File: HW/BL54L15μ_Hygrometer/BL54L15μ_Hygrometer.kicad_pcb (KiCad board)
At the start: 2 copper layers, 25.4 x 25.4 mm, 21 parts, among them IC1 nrf54L 453-00223R, J1 Conn_Qwiic, J2 Conn_ARM_JTAG_SWD_10, U1 nPM2100-QEXX, U2 SHT4x, U3 STCC4-D-R3, U5 BME688, X1 32.768 kHz

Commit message: BL54L15μ Hygrometer 2026v3
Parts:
- added JP1: VSET-GND, Jumper:SolderJumper-2_P1.3mm_Open_RoundedPad1.0x1.5mm, B.Cu at (103.9, 58.6)
- added SW1: Reset, Button_Switch_SMD:SW_Push_SPST_NO_Alps_SKRK, F.Cu at (102.3, 69.7)
- added TP1: VDD, TestPoint:TestPoint_Pad_D1.0mm, B.Cu at (108.0, 63.5)
- added TP10: PG/RESET, TestPoint:TestPoint_Pad_D1.0mm, B.Cu at (103.6, 66.8)
- added TP11: SYSGDEN, TestPoint:TestPoint_Pad_D1.0mm, B.Cu at (99.1, 66.8)
- added TP12: LED0, TestPoint:TestPoint_Pad_D1.0mm, B.Cu at (108.0, 74.2)
- added TP13: VDDSW, TestPoint:TestPoint_Pad_D1.0mm, B.Cu at (110.2, 63.5)
- added TP2: GND, TestPoint:TestPoint_Pad_1.0x1.0mm, B.Cu at (109.2, 101.6)
- added TP3: GPIO0/P0.01, TestPoint:TestPoint_Pad_D1.0mm, B.Cu at (93.5, 63.2)
- added TP4: GPIO1, TestPoint:TestPoint_Pad_D1.0mm, B.Cu at (101.1, 66.8)
- added TP5: SDA0/P1.14, TestPoint:TestPoint_Pad_D1.0mm, B.Cu at (96.3, 63.1)
- added TP6: SCL0/P1.04, TestPoint:TestPoint_Pad_D1.0mm, B.Cu at (98.3, 63.1)
- added TP7: SDA1/P1.06, TestPoint:TestPoint_Pad_D1.0mm, B.Cu at (103.6, 101.7)
- added TP8: SCL1/P1.08, TestPoint:TestPoint_Pad_D1.0mm, B.Cu at (106.4, 101.7)
- added TP9: SHPHLD, TestPoint:TestPoint_Pad_D1.0mm, B.Cu at (90.9, 63.2)
- BT1: footprint Battery:BatteryHolder_Keystone_2468_2xAAA -> BatteryHolder_Keystone_2468_2xAAA_NoHoles:BatteryHolder_Keystone_2468_2xAAA
- C1, C6: value 22μF -> 10μF
- IC1: footprint Ezurio 453-00223R:45300223R -> 453-00223R:45300223R
- X1: footprint Crystal:Crystal_SMD_2012-2Pin_2.0x1.2mm -> CM7V_T1A_LOW_ESR_32_768KHZ_9PF_20_TA_QC:XTAL_CM7V-T1A-LOW-ESR-32.768KHZ-9PF-20-TA-QC
- moved L1 30.5 mm to (100.0, 57.0), turned to 0 degrees
- moved C7 29.0 mm to (96.4, 98.5), turned to 0 degrees
- moved C2 28.7 mm to (102.7, 56.0), turned to -90 degrees
- moved J1 27.8 mm to (102.3, 107.1), turned to 180 degrees
- moved IC1 27.3 mm to (89.6, 82.0), turned to 180 degrees
- moved U2 27.2 mm to (95.9, 95.7)
- moved C1 26.9 mm to (104.3, 56.3), turned to -90 degrees
- moved U1 26.7 mm to (100.4, 61.0), turned to -90 degrees
- moved J2 26.5 mm to (93.8, 68.0), turned to 180 degrees
- moved C5 23.0 mm to (104.0, 60.4), turned to 90 degrees
- moved C6 21.4 mm to (105.7, 60.2), turned to 90 degrees
- moved C4 21.3 mm to (104.0, 62.5), turned to -90 degrees
- moved BT1 19.1 mm to (95.9, 58.1)
- moved R1 18.2 mm to (108.6, 67.6), turned to 0 degrees
- moved D1 15.0 mm to (108.6, 70.6), turned to 0 degrees
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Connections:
- net /NRESET renamed /~{RESET}
- D1 pad 2: /LED -> /LED0
- IC1 pad 1: /GPIO0 -> unconnected-(IC1-P2.05-Pad1)
- IC1 pad 13: /SWO -> unconnected-(IC1-P2.02-Pad13)
- IC1 pad 15: /SDA2 -> /LED0
- IC1 pad 17: /SCL2 -> /SCL0
- IC1 pad 18: /LED -> /SDA0
- IC1 pad 2: /SDA1 -> unconnected-(IC1-P2.00-Pad2)
- IC1 pad 29: unconnected-(IC1-P0.04/CLK-Pad29) -> /PG/RESET
- IC1 pad 3: unconnected-(IC1-P1.08/EXTREF/CLK16M/CLK-Pad3) -> /SCL1
- IC1 pad 35: unconnected-(IC1-P0.01-Pad35) -> /GPIO0
- IC1 pad 42: unconnected-(IC1-P2.07-Pad42) -> /SWO
- IC1 pad 43: /SCL1 -> unconnected-(IC1-P2.06/CLK-Pad43)
- IC1 pad 7: unconnected-(IC1-P1.06-Pad7) -> /SDA1
- J1 pad 3: /SDA2 -> /SDA1
- J1 pad 4: /SCL2 -> /SCL1
- U1 pad 1: unconnected-(U1-VSET-Pad1) -> /VSET
- U1 pad 10: unconnected-(U1-PG/RESET-Pad10) -> /PG/RESET
- U1 pad 4: unconnected-(U1-SHPHLD-Pad4) -> /SHPHLD
- U1 pad 6: /SDA1 -> /SDA0
- U1 pad 7: /SCL1 -> /SCL0
- U1 pad 8: unconnected-(U1-SYSGDEN-Pad8) -> /SYSGDEN
- U1 pad 9: unconnected-(U1-GPIO1-Pad9) -> /GPIO1
- U2 pad 1: /SDA1 -> /SDA0
- U2 pad 2: /SCL1 -> /SCL0
- U3 pad 1: /SCL2 -> /SCL1
- U3 pad 5: /SDA2 -> /SDA1
- U5 pad 3: /SDA2 -> /SDA1
- U5 pad 4: /SCL2 -> /SCL1
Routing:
- net VDDSW: track 29.7 -> 101.4 mm, vias 0 -> 1
- net /SDA0: track 0.00 -> 65.3 mm, vias 0 -> 3
- net /SCL0: track 0.00 -> 61.9 mm, vias 0 -> 3
- net VDD: track 38.7 -> 69.3 mm, vias 4 -> 6
- net /PG/RESET: track 0.00 -> 27.4 mm, vias 0 -> 3
- net /SDA2: track 26.6 -> 0.00 mm, vias 2 -> 0
- net /SCL2: track 24.8 -> 0.00 mm, vias 2 -> 0
- net /LED0: track 0.00 -> 21.9 mm, vias 0 -> 3
- net /SCL1: track 39.3 -> 53.9 mm, vias 0 -> 3
- net /SHPHLD: track 0.00 -> 10.3 mm, vias 0 -> 1
- net /LED: track 9.51 -> 0.00 mm
- net /VBAT: track 20.6 -> 12.9 mm
- net /SDA1: track 39.3 -> 46.1 mm, vias 2 -> 5
- net /SWO: track 12.4 -> 18.2 mm
- net /~{RESET}: track 12.8 -> 18.6 mm
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- removed copper zone on F.Cu, net VDDSW
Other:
- board size 25.4 x 25.4 mm -> 25.4 x 55.9 mm
- board text added: "${TITLE} nRF54L15 MCU"
- board text added: "BME688 Pressure/Gas I²C 0x76 P1.06/P1.08"
- board text added: "Battery PMIC"
- board text added: "CO_{2} Sensor"
- board text added: "Gas Sensor"
- board text added: "Hot loop: VBAT -> SW -> VINT -> PVSS (VBAT GND)"
- board text added: "Humidity and Temp Sensor"
- board text added: "I²C Connector STEMMA QT SDA P1.06 SCL P1.08 Load switched"
- board text added: "I²C0 SDA P1.14 SCL P1.04 I²C1 SDA P1.06 SCL P1.08 I²C0 VDD, I²C1 nPM2100 LS MCU 13k pull-ups required"
- board text added: "Reset"
- board text added: "SHT4x Humidity/temp I²C 0x44 P1.14/P1.04 Thermal cutout"
- board text added: "STCC4 CO₂±(100 ppm + 10%) I²C 0x64 P1.06/P1.08"
- board text added: "Status"
- board text added: "nPM2100 I²C 0x74 SDA P1.14 SCL P1.04"
- board text added: "nrf54L15 MCU BLE/Thread/Zigbee"
- board text removed: "BL54L15μ: nrf54L15 MCU module nPM2100: bat .7-3.4V, I2C1 0x74 SHT4x: Humidity/temp, I2C1 0x44 STCC4: C02, min 2.7V, I2C2 0x64 BME688: Pressure/Gas, I2C2 0x76 Qwiic I2C receptable on bus 2"
- board text removed: "LED"

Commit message: Cleanup Hygrometer BOM
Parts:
- C3: value 10uF -> 10μF
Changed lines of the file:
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@@
 			)
 		)
-		(property "Value" "10uF"
+		(property "Value" "10μF"
 			(at 0 1.43 90)
 			(layer "F.Fab")
@@
 		(sheetname "/")
 		(sheetfile "BL54L15μ_Hygrometer.kicad_sch")
-		(attr exclude_from_pos_files)
+		(attr exclude_from_pos_files exclude_from_bom)
 		(fp_circle
 			(center 0 0)
@@
 		(sheetname "/")
 		(sheetfile "BL54L15μ_Hygrometer.kicad_sch")
-		(attr exclude_from_pos_files)
+		(attr exclude_from_pos_files exclude_from_bom)
 		(fp_circle
 			(center 0 0)
@@
 		(sheetname "/")
 		(sheetfile "BL54L15μ_Hygrometer.kicad_sch")
-		(attr exclude_from_pos_files)
+		(attr exclude_from_pos_files exclude_from_bom)
 		(fp_line
 			(start -0.7 0.7)
@@
 		(sheetname "/")
 		(sheetfile "BL54L15μ_Hygrometer.kicad_sch")
-		(attr exclude_from_pos_files)
+		(attr exclude_from_pos_files exclude_from_bom)
 		(fp_circle
 			(center 0 0)
@@
 		(sheetname "/")
 		(sheetfile "BL54L15μ_Hygrometer.kicad_sch")
-		(attr exclude_from_pos_files)
+		(attr exclude_from_pos_files exclude_from_bom)
 		(fp_circle
 			(center 0 0)
@@
 		(sheetname "/")
 		(sheetfile "BL54L15μ_Hygrometer.kicad_sch")
-		(attr exclude_from_pos_files)
+		(attr exclude_from_pos_files exclude_from_bom)
 		(fp_circle
 			(center 0 0)
@@
 		(sheetname "/")
 		(sheetfile "BL54L15μ_Hygrometer.kicad_sch")
-		(attr exclude_from_pos_files)
+		(attr exclude_from_pos_files exclude_from_bom)
 		(fp_circle
 			(center 0 0)
@@
 		(sheetname "/")
 		(sheetfile "BL54L15μ_Hygrometer.kicad_sch")
-		(attr exclude_from_pos_files)
+		(attr exclude_from_pos_files exclude_from_bom)
 		(fp_circle
 			(center 0 0)
@@
 		(sheetname "/")
 		(sheetfile "BL54L15μ_Hygrometer.kicad_sch")
-		(attr exclude_from_pos_files)
+		(attr exclude_from_pos_files exclude_from_bom)
 		(fp_circle
 			(center 0 0)
@@
 		(sheetname "/")
 		(sheetfile "BL54L15μ_Hygrometer.kicad_sch")
-		(attr exclude_from_pos_files)
+		(attr exclude_from_pos_files exclude_from_bom)
 		(fp_circle
 			(center 0 0)
@@
 		(sheetfile "BL54L15μ_Hygrometer.kicad_sch")
 		(zone_connect 1)
-		(attr exclude_from_pos_files allow_soldermask_bridges)
+		(attr exclude_from_pos_files exclude_from_bom allow_soldermask_bridges)
 		(fp_rect
 			(start -0.15 0.75)
@@
 		(sheetname "/")
 		(sheetfile "BL54L15μ_Hygrometer.kicad_sch")
-		(attr exclude_from_pos_files)
+		(attr exclude_from_pos_files exclude_from_bom)
 		(fp_circle
 			(center 0 0)
@@
 		(sheetname "/")
 		(sheetfile "BL54L15μ_Hygrometer.kicad_sch")
-		(attr exclude_from_pos_files)
+		(attr exclude_from_pos_files exclude_from_bom)
 		(fp_circle
 			(center 0 0)
@@
 		(sheetname "/")
 		(sheetfile "BL54L15μ_Hygrometer.kicad_sch")
-		(attr exclude_from_pos_files)
+		(attr exclude_from_pos_files exclude_from_bom)
 		(fp_circle
 			(center 0 0)

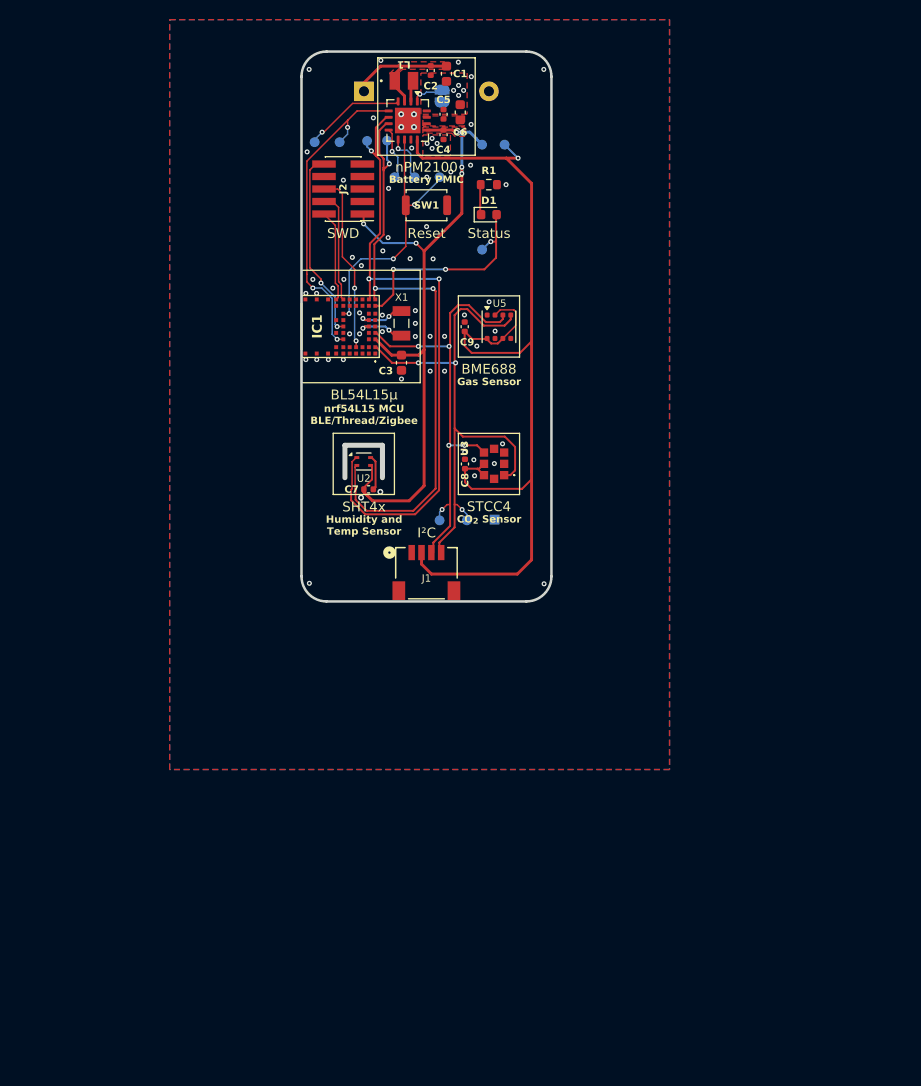
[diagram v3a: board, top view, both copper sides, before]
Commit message: BL54L15μ Hygrometer 2026v4 with leak sensing
- Switch to CR2 battery
- Drop power-hungry STCC4/BME688 sensors
- Circular design with M1.2 mounting holes
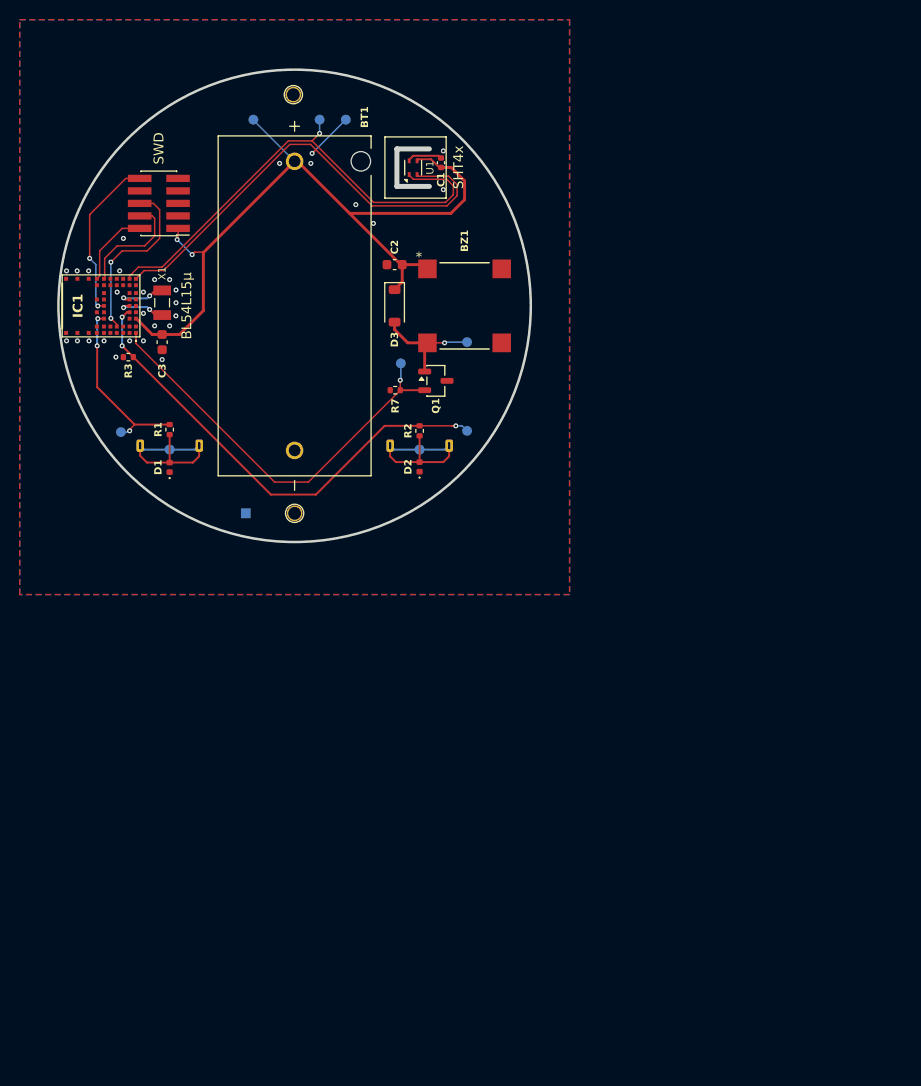
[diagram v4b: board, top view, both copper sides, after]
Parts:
- removed the C1 at (104.3, 56.3)
- removed C4: 2.2μF, Capacitor_SMD:C_0402_1005Metric
- removed C5, C8, C9: 100nF, Capacitor_SMD:C_0402_1005Metric
- removed C6: 10μF, Capacitor_SMD:C_0603_1608Metric
- removed the J1 at (102.3, 107.1)
- removed JP1: VSET-GND, Jumper:SolderJumper-2_P1.3mm_Open_RoundedPad1.0x1.5mm
- removed L1: 2.2μH, CIGT201610EH2R2MNE:IND_CIGT2016_SAM
- removed SW1: Reset, Button_Switch_SMD:SW_Push_SPST_NO_Alps_SKRK
- removed TP11: SYSGDEN, TestPoint:TestPoint_Pad_D1.0mm
- removed TP12: LED0, TestPoint:TestPoint_Pad_D1.0mm
- removed TP13: VDDSW, TestPoint:TestPoint_Pad_D1.0mm
- removed TP3: GPIO0/P0.01, TestPoint:TestPoint_Pad_D1.0mm
- removed TP4: GPIO1, TestPoint:TestPoint_Pad_D1.0mm
- removed the U1 at (100.4, 61.0)
- removed U3: STCC4-D-R3, STCC4-D-R3:STCC4DR3
- removed U5: BME688, Package_LGA:Bosch_LGA-8_3x3mm_P0.8mm_ClockwisePinNumbering
- added BZ1: Buzzer, AST0827MW-03BTRQ:AST0827MW-03BTRQ_MAL, F.Cu at (106.2, 79.9)
- added D2: 5V TVS, Diode_SMD:D_0402_1005Metric, F.Cu at (101.6, 96.2)
- added D3: MBR0520L, Diode_SMD:D_SOD-123, F.Cu at (99.1, 79.9)
- added H1: MountingHole, MountingHoleCompact:MountingHole_M1.2_1.3mm_Plated, F.Cu at (88.8, 58.4)
- added H2: MountingHole, MountingHoleCompact:MountingHole_M1.2_1.3mm_Plated, F.Cu at (88.9, 101.0)
- added P1: 6mmMetalDome, MetalDomeSwitch:TriangleDome_Diameter6mm, B.Cu at (76.2, 94.5)
- added P2: 6mmMetalDome, MetalDomeSwitch:TriangleDome_Diameter6mm, B.Cu at (101.6, 94.5)
- added Q1: NMOS, Package_TO_SOT_SMD:SOT-23-3, F.Cu at (103.3, 87.5)
- added R2: 10kΩ, Resistor_SMD:R_0402_1005Metric, F.Cu at (101.6, 92.6)
- added R3: 1MΩ, Resistor_SMD:R_0402_1005Metric, F.Cu at (72.0, 85.1)
- added R7: 1MΩ, Resistor_SMD:R_0402_1005Metric, F.Cu at (99.1, 88.5)
- BT1: footprint BatteryHolder_Keystone_2468_2xAAA_NoHoles:BatteryHolder_Keystone_2468_2xAAA -> 1011:BAT_1011; moved to F.Cu
- C2: value 100nF -> 10μF; footprint Capacitor_SMD:C_0402_1005Metric -> Capacitor_SMD:C_0603_1608Metric
- D1: value PWRLED -> 5V TVS; footprint LED_SMD:LED_0603_1608Metric -> Diode_SMD:D_0402_1005Metric
- R1: value 100Ω -> 10kΩ; footprint Resistor_SMD:R_0603_1608Metric -> Resistor_SMD:R_0402_1005Metric
- TP10: value PG/RESET -> BUZZER
- TP5: value SDA0/P1.14 -> SDA
- TP6: value SCL0/P1.04 -> SCL
- TP7: value SDA1/P1.06 -> SIREN
- TP8: value SCL1/P1.08 -> LEAK_DRIVE
- TP9: value SHPHLD -> LEAK_SENSE
- moved D1 41.4 mm to (76.2, 96.3), turned to 90 degrees
- moved R1 40.9 mm to (76.2, 92.5), turned to 90 degrees
- moved TP8 36.3 mm to (71.2, 92.7)
- moved C1 34.0 mm to (103.8, 65.3), turned to 90 degrees
- moved TP9 33.2 mm to (106.4, 92.6)
- moved U1 30.3 mm to (100.9, 65.8), turned to 90 degrees
- moved TP2 25.3 mm to (83.9, 101.0), turned to 180 degrees
- moved C3 24.4 mm to (75.4, 83.6)
- moved IC1 24.4 mm to (65.3, 79.9)
- moved X1 24.4 mm to (75.4, 79.6)
- moved TP1 23.4 mm to (84.7, 61.0), turned to 180 degrees
- moved BT1 22.9 mm to (88.9, 79.9)
- moved C2 20.1 mm to (99.1, 75.7), turned to 180 degrees
- moved J1 18.8 mm to (75.1, 69.5)
- moved TP10 17.0 mm to (106.4, 83.6), turned to 180 degrees
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- renumbered C7 to C1, J2 to J1, U2 to U1
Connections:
- net /SCL0 renamed /SCL
- net /SDA0 renamed /SDA
- BT1 pad 1: /VBAT -> VDD
- C2 pad 1: /VBAT -> VDD
- D1 pad 1: Net-(D1-K) -> GND
- D1 pad 2: /LED0 -> Net-(D1-A2)
- IC1 pad 1: unconnected-(IC1-P2.05-Pad1) -> /SIREN
- IC1 pad 15: /LED0 -> unconnected-(IC1-P1.05-Pad15)
- IC1 pad 29: /PG/RESET -> unconnected-(IC1-P0.04/CLK-Pad29)
- IC1 pad 3: /SCL1 -> unconnected-(IC1-P1.08/EXTREF/CLK16M/CLK-Pad3)
- IC1 pad 35: /GPIO0 -> /LEAK_DRIVE
- IC1 pad 7: /SDA1 -> unconnected-(IC1-P1.06-Pad7)
- IC1 pad 8: unconnected-(IC1-P1.07-Pad8) -> /LEAK_SENSE
- R1 pad 1: Net-(D1-K) -> Net-(D1-A2)
- R1 pad 2: GND -> /LEAK_DRIVE
- TP10 pad 1: /PG/RESET -> /BUZZER
- TP7 pad 1: /SDA1 -> /SIREN
- TP8 pad 1: /SCL1 -> /LEAK_DRIVE
- TP9 pad 1: /SHPHLD -> /LEAK_SENSE
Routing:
- net VDDSW: track 101.4 -> 0.00 mm, vias 1 -> 0
- net /SCL1: track 53.9 -> 0.00 mm, vias 3 -> 0
- net /LEAK_SENSE: track 0.00 -> 48.3 mm, vias 0 -> 3
- net /SDA1: track 46.1 -> 0.00 mm, vias 5 -> 0
- net /SIREN: track 0.00 -> 43.0 mm, vias 0 -> 1
- net /GPIO0: track 33.5 -> 0.00 mm, vias 3 -> 0
- net /PG/RESET: track 27.4 -> 0.00 mm, vias 3 -> 0
- net /LED0: track 21.9 -> 0.00 mm, vias 3 -> 0
- net /LEAK_DRIVE: track 0.00 -> 18.3 mm, vias 0 -> 3
- net Net-(D1-A2): track 0.00 -> 17.8 mm
- net Net-(D2-A2): track 0.00 -> 17.6 mm
- net /SDA: track 65.3 -> 50.1 mm, vias 3 -> 1
- net /VBAT: track 12.9 -> 0.00 mm
- net /BUZZER: track 0.00 -> 11.7 mm, vias 0 -> 1
- net /SHPHLD: track 10.3 -> 0.00 mm, vias 1 -> 0
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- removed copper zone on F.Cu, net /VBAT
- removed copper zone on F.Cu, net /VINT
- removed copper zone on F.Cu, net VDD
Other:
- board size 25.4 x 55.9 mm -> 48 x 48 mm
- board text added: "${TITLE} Power - CR2 battery, no PMIC SHT4x - Humidity and temperature sensor P1/P2 - Contact points for leak sensor probes"
- board text added: "Daniel Stiner ${REVISION}"
- board text added: "nRF54L15 MCU"
- board text removed: "${TITLE} Daniel Stiner ${REVISION}"
- board text removed: "${TITLE} nRF54L15 MCU"
- board text removed: "BME688"
- board text removed: "BME688 Pressure/Gas I²C 0x76 P1.06/P1.08"
- board text removed: "Battery PMIC"
- board text removed: "CO_{2} Sensor"
- board text removed: "Gas Sensor"
- board text removed: "Hot loop: VBAT -> SW -> VINT -> PVSS (VBAT GND)"
- board text removed: "Humidity and Temp Sensor"
- board text removed: "I²C"
- board text removed: "I²C Connector STEMMA QT SDA P1.06 SCL P1.08 Load switched"
- board text removed: "I²C0 SDA P1.14 SCL P1.04 I²C1 SDA P1.06 SCL P1.08 I²C0 VDD, I²C1 nPM2100 LS MCU 13k pull-ups required"
- board text removed: "Reset"
- board text removed: "SHT4x Humidity/temp I²C 0x44 P1.14/P1.04 Thermal cutout"
- board text removed: "STCC4"
- board text removed: "STCC4 CO₂±(100 ppm + 10%) I²C 0x64 P1.06/P1.08"
- board text removed: "Status"
- board text removed: "nPM2100"
- board text removed: "nPM2100 I²C 0x74 SDA P1.14 SCL P1.04"
- board text removed: "nrf54L15 MCU BLE/Thread/Zigbee"
